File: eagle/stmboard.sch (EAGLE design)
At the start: 23 parts, among them IC1 LD117AS12TR

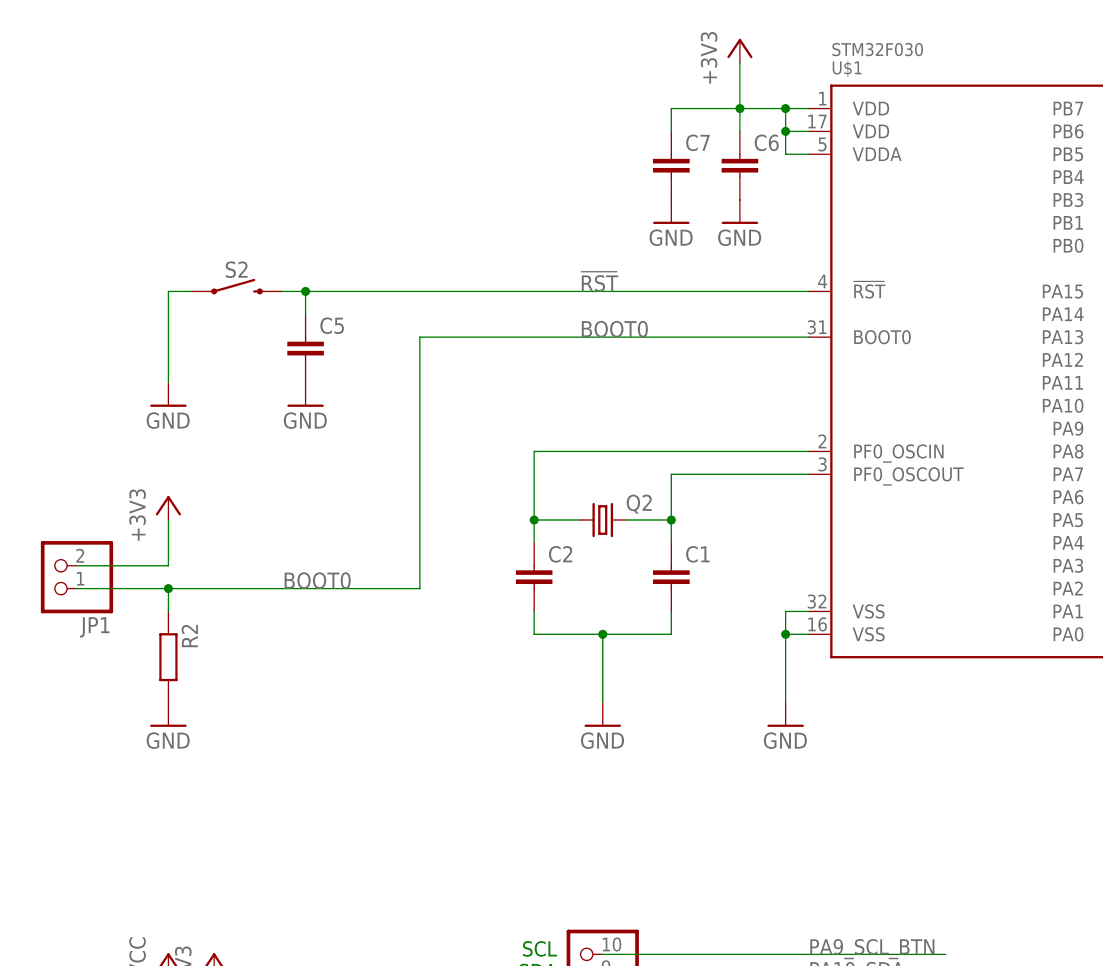
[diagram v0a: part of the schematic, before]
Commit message: changed boot0 jumper to 3-pin
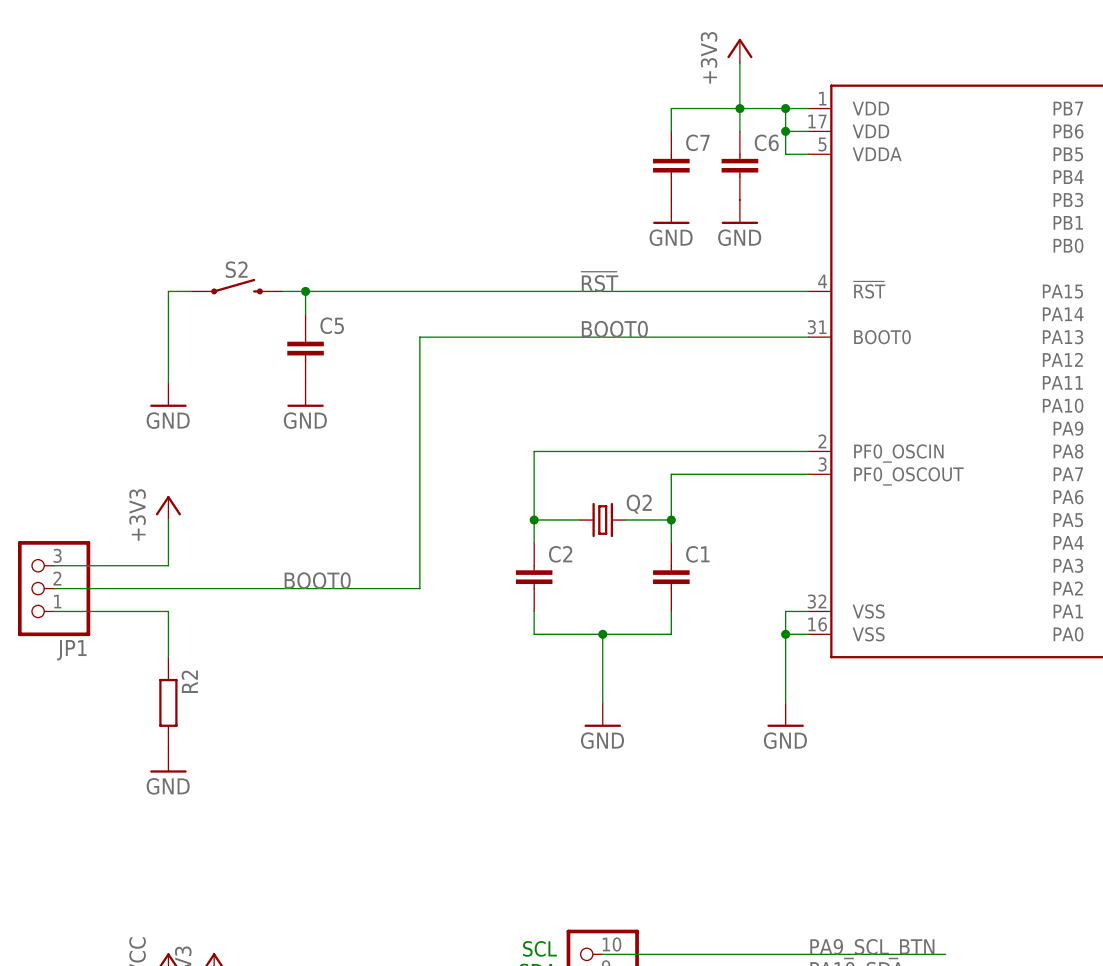
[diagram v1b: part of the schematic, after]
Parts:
- JP1: device pinhead:PINHD-1X2 -> pinhead:PINHD-1X3
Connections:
- new net N$3: JP1.1, R2.1
- net +3V3: now also JP1.3; no longer JP1.2
- net BOOT0: now also JP1.2; no longer JP1.1, R2.1
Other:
- moved on the sheet: R2

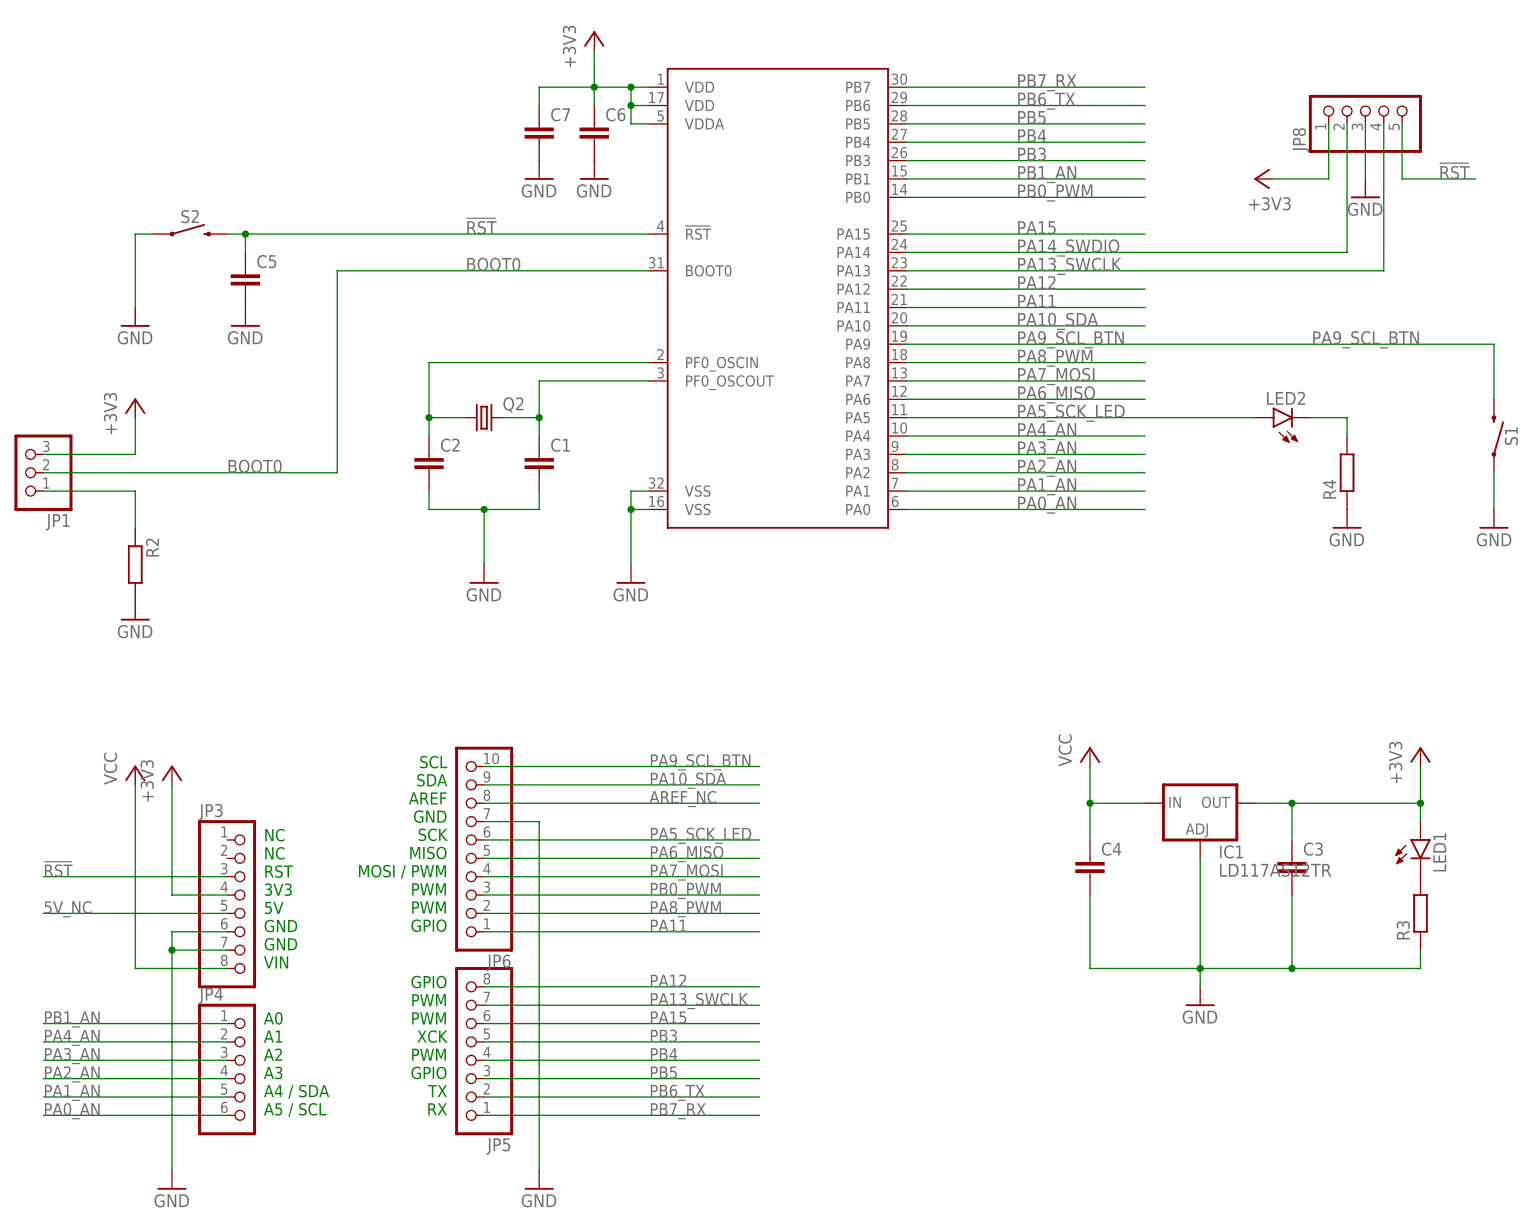
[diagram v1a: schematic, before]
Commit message: added part values
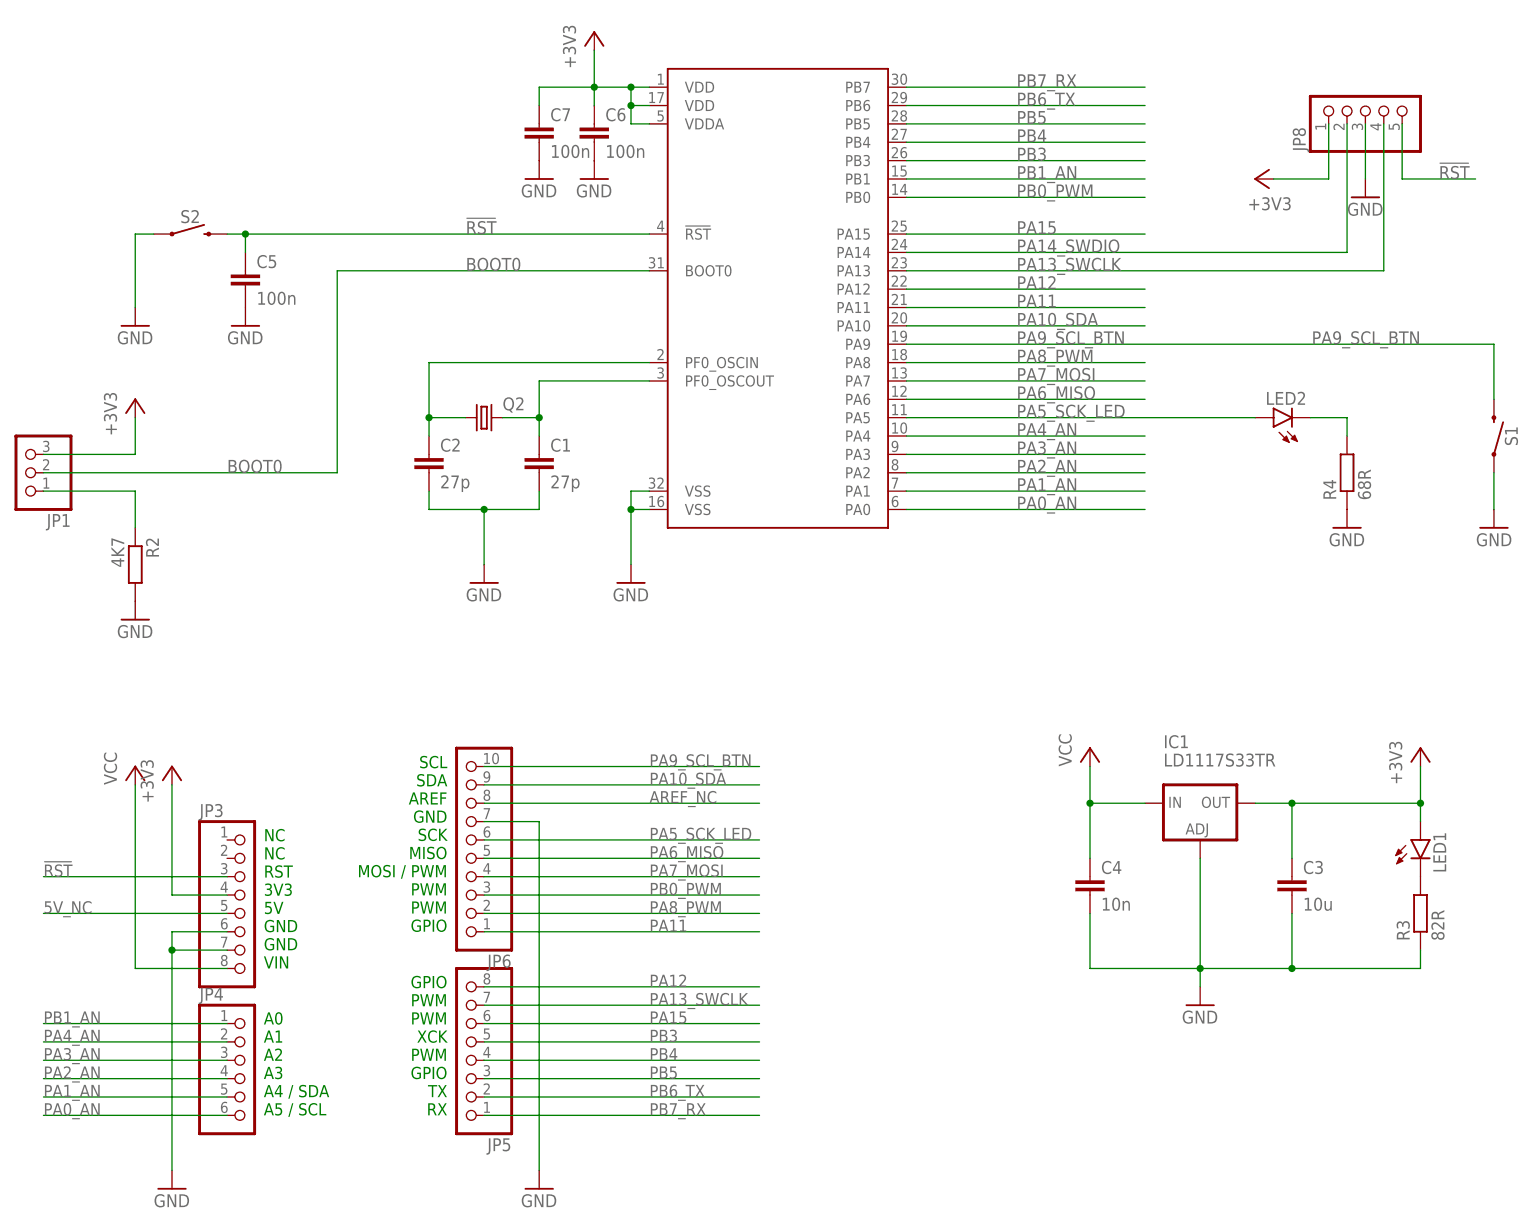
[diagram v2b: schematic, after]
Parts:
- C1, C2: value (none) -> 27p
- C3: value (none) -> 10u
- C4: value (none) -> 10n
- C5, C6, C7: value (none) -> 100n
- IC1: value LD117AS12TR -> LD1117S33TR
- R2: value (none) -> 4K7
- R3: value (none) -> 82R
- R4: value (none) -> 68R
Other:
- moved on the sheet: C3, C4
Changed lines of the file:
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@@
 <parts>
 <part name="U$1" library="stm32F030x" deviceset="STM32F030" device="" package3d_urn="urn:adsk.eagle:package:4313/2"/>
-<part name="C1" library="rcl" deviceset="C-EU" device="C1206"/>
-<part name="C2" library="rcl" deviceset="C-EU" device="C1206"/>
+<part name="C1" library="rcl" deviceset="C-EU" device="C1206" value="27p"/>
+<part name="C2" library="rcl" deviceset="C-EU" device="C1206" value="27p"/>
 <part name="GND1" library="supply1" deviceset="GND" device=""/>
 <part name="GND2" library="supply1" deviceset="GND" device=""/>
-<part name="IC1" library="v-reg" deviceset="LD117A?*" device="S" technology="12TR"/>
+<part name="IC1" library="v-reg" deviceset="LD117A?*" device="S" technology="12TR" value="LD1117S33TR"/>
 <part name="GND3" library="supply1" deviceset="GND" device=""/>
-<part name="C3" library="rcl" deviceset="C-EU" device="C1206K"/>
-<part name="C4" library="rcl" deviceset="C-EU" device="C1206K"/>
+<part name="C3" library="rcl" deviceset="C-EU" device="C1206K" value="10u"/>
+<part name="C4" library="rcl" deviceset="C-EU" device="C1206K" value="10n"/>
 <part name="+3V1" library="supply1" deviceset="+3V3" device=""/>
 <part name="P+1" library="supply1" deviceset="VCC" device=""/>
 <part name="+3V2" library="supply1" deviceset="+3V3" device=""/>
-<part name="C5" library="rcl" deviceset="C-EU" device="C1206K"/>
+<part name="C5" library="rcl" deviceset="C-EU" device="C1206K" value="100n"/>
 <part name="GND4" library="supply1" deviceset="GND" device=""/>
 <part name="GND5" library="supply1" deviceset="GND" device=""/>
-<part name="C6" library="rcl" deviceset="C-EU" device="C1206K"/>
+<part name="C6" library="rcl" deviceset="C-EU" device="C1206K" value="100n"/>
 <part name="GND6" library="supply1" deviceset="GND" device=""/>
-<part name="R2" library="rcl" deviceset="R-EU_" device="M1206"/>
+<part name="R2" library="rcl" deviceset="R-EU_" device="M1206" value="4K7"/>
 <part name="+3V4" library="supply1" deviceset="+3V3" device=""/>
 <part name="GND7" library="supply1" deviceset="GND" device=""/>
 <part name="Q2" library="crystal" deviceset="CRYSTAL" device="SM49"/>
-<part name="C7" library="rcl" deviceset="C-EU" device="C1206K"/>
+<part name="C7" library="rcl" deviceset="C-EU" device="C1206K" value="100n"/>
 <part name="GND8" library="supply1" deviceset="GND" device=""/>
 <part name="S2" library="SparkFun-Switches" deviceset="MOMENTARY-SWITCH-SPST" device="-SMD-6.0X3.5MM" value=""/>
@@
 <part name="+3V7" library="supply1" deviceset="+3V3" device=""/>
 <part name="LED1" library="led" library_urn="urn:adsk.eagle:library:259" deviceset="LED" device="SMT1206" package3d_urn="urn:adsk.eagle:package:15796/2"/>
-<part name="R3" library="rcl" deviceset="R-EU_" device="M1206"/>
+<part name="R3" library="rcl" deviceset="R-EU_" device="M1206" value="82R"/>
 <part name="LED2" library="led" library_urn="urn:adsk.eagle:library:259" deviceset="LED" device="SMT1206" package3d_urn="urn:adsk.eagle:package:15796/2"/>
-<part name="R4" library="rcl" deviceset="R-EU_" device="M1206"/>
+<part name="R4" library="rcl" deviceset="R-EU_" device="M1206" value="68R"/>
 <part name="GND9" library="supply1" deviceset="GND" device=""/>
 <part name="GND14" library="supply1" deviceset="GND" device=""/>
@@
 </instance>
 <instance part="IC1" gate="G$1" x="469.9" y="22.86" smashed="yes">
-<attribute name="NAME" x="472.44" y="15.24" size="1.778" layer="95"/>
-<attribute name="VALUE" x="472.44" y="12.7" size="1.778" layer="96"/>
+<attribute name="NAME" x="464.82" y="30.48" size="1.778" layer="95"/>
+<attribute name="VALUE" x="464.82" y="27.94" size="1.778" layer="96"/>
 </instance>
 <instance part="GND3" gate="1" x="469.9" y="-5.08" smashed="yes">
 <attribute name="VALUE" x="467.36" y="-7.62" size="1.778" layer="96"/>
 </instance>
-<instance part="C3" gate="G$1" x="482.6" y="15.24" smashed="yes">
-<attribute name="NAME" x="484.124" y="15.621" size="1.778" layer="95"/>
-<attribute name="VALUE" x="484.124" y="10.541" size="1.778" layer="96"/>
-</instance>
-<instance part="C4" gate="G$1" x="454.66" y="15.24" smashed="yes">
-<attribute name="NAME" x="456.184" y="15.621" size="1.778" layer="95"/>
-<attribute name="VALUE" x="456.184" y="10.541" size="1.778" layer="96"/>
+<instance part="C3" gate="G$1" x="482.6" y="12.7" smashed="yes">
+<attribute name="NAME" x="484.124" y="13.081" size="1.778" layer="95"/>
+<attribute name="VALUE" x="484.124" y="8.001" size="1.778" layer="96"/>
+</instance>
+<instance part="C4" gate="G$1" x="454.66" y="12.7" smashed="yes">
+<attribute name="NAME" x="456.184" y="13.081" size="1.778" layer="95"/>
+<attribute name="VALUE" x="456.184" y="8.001" size="1.778" layer="96"/>
 </instance>
 <instance part="+3V1" gate="G$1" x="500.38" y="30.48" smashed="yes">
@@
 <segment>
 <pinref part="C4" gate="G$1" pin="2"/>
-<wire x1="454.66" y1="10.16" x2="454.66" y2="0" width="0.1524" layer="91"/>
+<wire x1="454.66" y1="7.62" x2="454.66" y2="0" width="0.1524" layer="91"/>
 <wire x1="454.66" y1="0" x2="469.9" y2="0" width="0.1524" layer="91"/>
 <pinref part="C3" gate="G$1" pin="2"/>
 <wire x1="469.9" y1="0" x2="482.6" y2="0" width="0.1524" layer="91"/>
-<wire x1="482.6" y1="0" x2="482.6" y2="10.16" width="0.1524" layer="91"/>
+<wire x1="482.6" y1="0" x2="482.6" y2="7.62" width="0.1524" layer="91"/>
 <pinref part="IC1" gate="G$1" pin="ADJ"/>
 <wire x1="469.9" y1="15.24" x2="469.9" y2="0" width="0.1524" layer="91"/>
@@
 <segment>
 <pinref part="C4" gate="G$1" pin="1"/>
-<wire x1="454.66" y1="17.78" x2="454.66" y2="22.86" width="0.1524" layer="91"/>
+<wire x1="454.66" y1="15.24" x2="454.66" y2="22.86" width="0.1524" layer="91"/>
 <pinref part="IC1" gate="G$1" pin="IN"/>
 <wire x1="454.66" y1="22.86" x2="462.28" y2="22.86" width="0.1524" layer="91"/>
@@
 <wire x1="500.38" y1="22.86" x2="500.38" y2="20.32" width="0.1524" layer="91"/>
 <pinref part="C3" gate="G$1" pin="1"/>
-<wire x1="482.6" y1="17.78" x2="482.6" y2="22.86" width="0.1524" layer="91"/>
+<wire x1="482.6" y1="15.24" x2="482.6" y2="22.86" width="0.1524" layer="91"/>
 <junction x="482.6" y="22.86"/>
 </segment>
